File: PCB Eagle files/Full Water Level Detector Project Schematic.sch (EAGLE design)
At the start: 25 parts, among them IC1 74AHCT125, J1 Sensor 1, J2 Sensor 2, J3 Servo

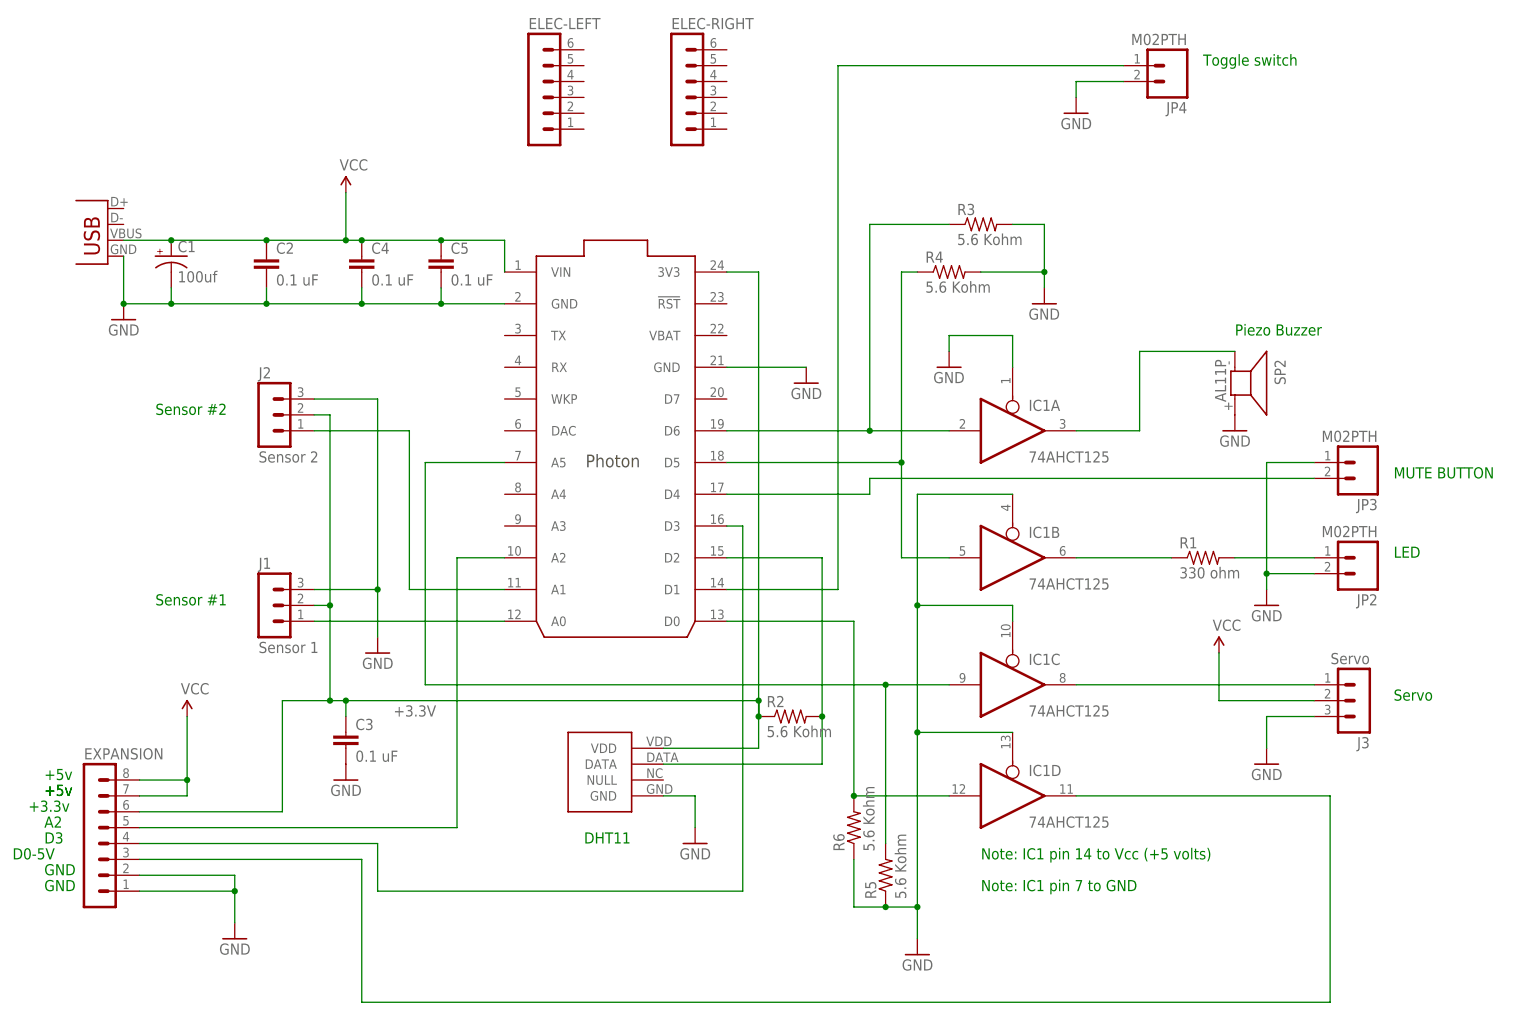
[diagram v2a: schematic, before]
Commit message: Optimized and routed PCB
Still must perform the ground pour and create silk screen.
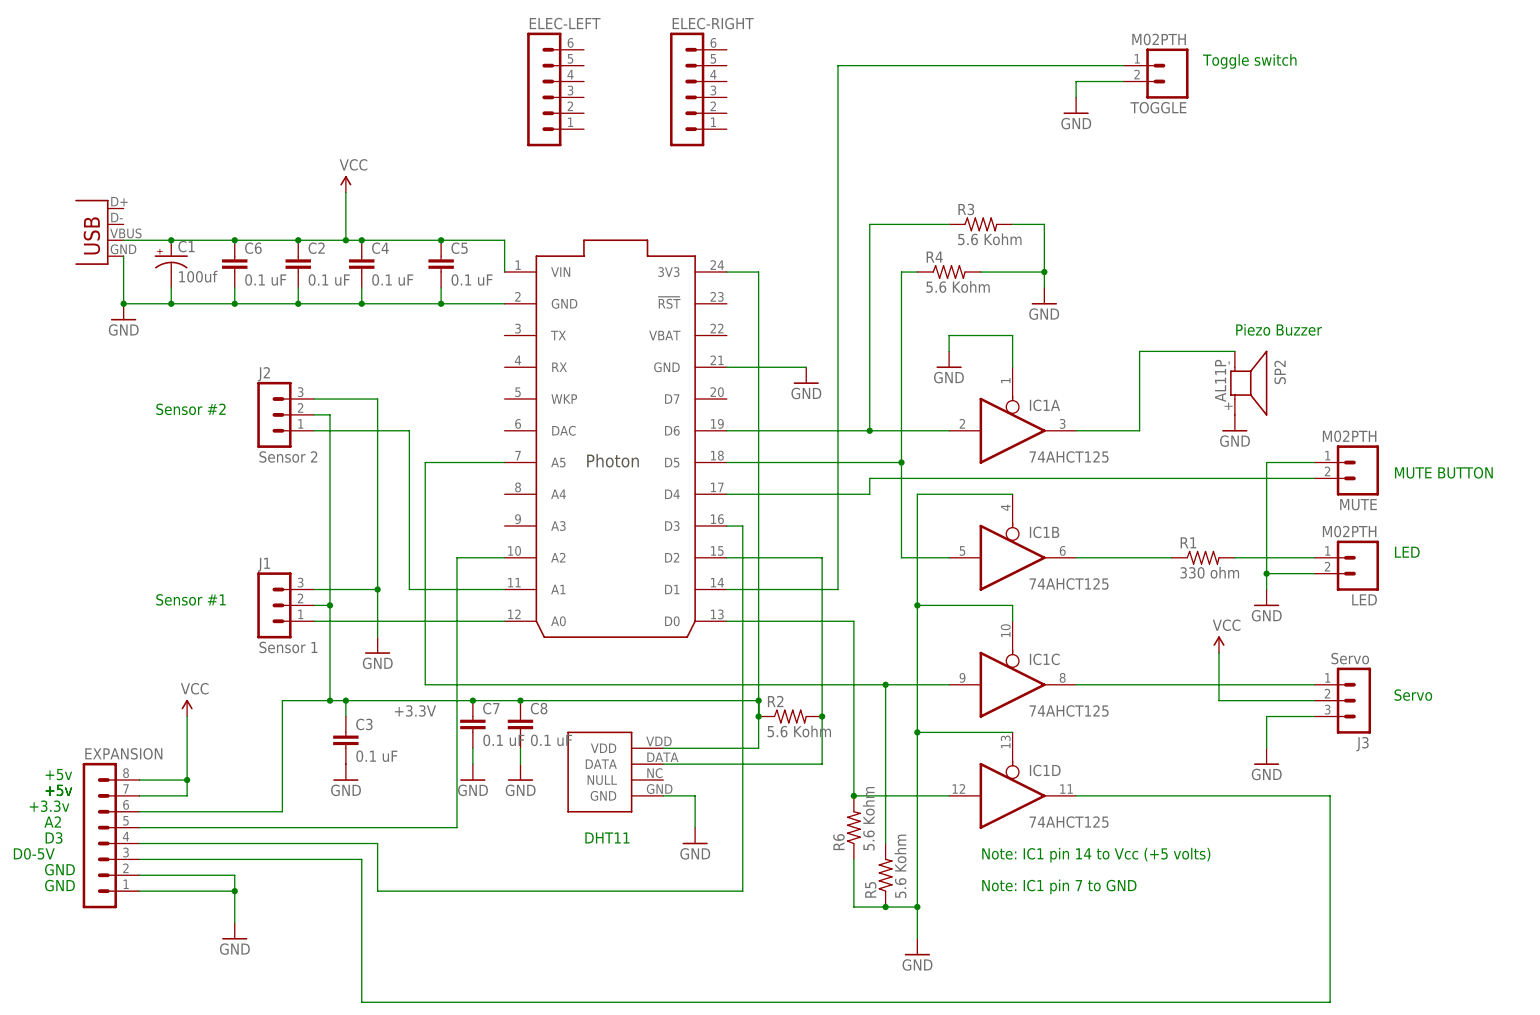
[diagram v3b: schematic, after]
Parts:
- added C6, C7, C8: 0.1 uF, SparkFun-Passives:CAPPTH
- renumbered JP2 to LED, JP3 to MUTE, JP4 to TOGGLE
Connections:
- net +3.3V: now also C7.1, C8.1
- net GND: now also C6.2, C7.2, C8.2
- net VCC: now also C6.1
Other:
- moved on the sheet: C2
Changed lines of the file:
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@@
 <part name="ELEC-LEFT" library="con-lstb" deviceset="MA06-1" device=""/>
 <part name="ELEC-RIGHT" library="con-lstb" deviceset="MA06-1" device=""/>
-<part name="JP3" library="SparkFun-Connectors" deviceset="M02" device="PTH"/>
-<part name="JP2" library="SparkFun-Connectors" deviceset="M02" device="PTH"/>
-<part name="JP4" library="SparkFun-Connectors" deviceset="M02" device="PTH"/>
+<part name="MUTE" library="SparkFun-Connectors" deviceset="M02" device="PTH"/>
+<part name="LED" library="SparkFun-Connectors" deviceset="M02" device="PTH"/>
+<part name="TOGGLE" library="SparkFun-Connectors" deviceset="M02" device="PTH"/>
+<part name="C6" library="SparkFun-Passives" deviceset="CAP" device="PTH" value="0.1 uF"/>
+<part name="C7" library="SparkFun-Passives" deviceset="CAP" device="PTH" value="0.1 uF"/>
+<part name="C8" library="SparkFun-Passives" deviceset="CAP" device="PTH" value="0.1 uF"/>
+<part name="GND14" library="SparkFun-Aesthetics" deviceset="GND" device=""/>
+<part name="GND15" library="SparkFun-Aesthetics" deviceset="GND" device=""/>
 </parts>
 <sheets>
@@
 <instance part="JP1" gate="G$1" x="-88.9" y="96.52" rot="MR0"/>
 <instance part="GND2" gate="1" x="-86.36" y="86.36" rot="MR0"/>
-<instance part="C2" gate="G$1" x="-63.5" y="93.98"/>
+<instance part="C2" gate="G$1" x="-58.42" y="93.98"/>
 <instance part="C3" gate="G$1" x="-50.8" y="17.78"/>
 <instance part="GND3" gate="1" x="-50.8" y="12.7" rot="MR0"/>
@@
 <instance part="ELEC-LEFT" gate="1" x="-20.32" y="124.46"/>
 <instance part="ELEC-RIGHT" gate="1" x="2.54" y="124.46"/>
-<instance part="JP3" gate="G$1" x="111.76" y="63.5" rot="R180"/>
-<instance part="JP2" gate="G$1" x="111.76" y="48.26" rot="R180"/>
-<instance part="JP4" gate="G$1" x="81.28" y="127" rot="R180"/>
+<instance part="MUTE" gate="G$1" x="111.76" y="63.5" rot="R180"/>
+<instance part="LED" gate="G$1" x="111.76" y="48.26" rot="R180"/>
+<instance part="TOGGLE" gate="G$1" x="81.28" y="127" rot="R180"/>
+<instance part="C6" gate="G$1" x="-68.58" y="93.98"/>
+<instance part="C7" gate="G$1" x="-30.48" y="20.32"/>
+<instance part="C8" gate="G$1" x="-22.86" y="20.32"/>
+<instance part="GND14" gate="1" x="-30.48" y="12.7" rot="MR0"/>
+<instance part="GND15" gate="1" x="-22.86" y="12.7" rot="MR0"/>
 </instances>
 <busses>
@@
 <pinref part="JP1" gate="G$1" pin="GND"/>
 <wire x1="-25.4" y1="88.9" x2="-35.56" y2="88.9" width="0.1524" layer="91"/>
-<wire x1="-48.26" y1="88.9" x2="-63.5" y2="88.9" width="0.1524" layer="91"/>
-<wire x1="-63.5" y1="88.9" x2="-78.74" y2="88.9" width="0.1524" layer="91"/>
+<wire x1="-48.26" y1="88.9" x2="-58.42" y2="88.9" width="0.1524" layer="91"/>
+<wire x1="-58.42" y1="88.9" x2="-68.58" y2="88.9" width="0.1524" layer="91"/>
+<wire x1="-68.58" y1="88.9" x2="-78.74" y2="88.9" width="0.1524" layer="91"/>
 <wire x1="-78.74" y1="88.9" x2="-86.36" y2="88.9" width="0.1524" layer="91"/>
 <wire x1="-86.36" y1="88.9" x2="-86.36" y2="96.52" width="0.1524" layer="91"/>
@@
 <junction x="-86.36" y="88.9"/>
 <pinref part="C2" gate="G$1" pin="2"/>
-<wire x1="-63.5" y1="91.44" x2="-63.5" y2="88.9" width="0.1524" layer="91"/>
-<junction x="-63.5" y="88.9"/>
+<wire x1="-58.42" y1="91.44" x2="-58.42" y2="88.9" width="0.1524" layer="91"/>
+<junction x="-58.42" y="88.9"/>
 <pinref part="C4" gate="G$1" pin="2"/>
 <wire x1="-48.26" y1="91.44" x2="-48.26" y2="88.9" width="0.1524" layer="91"/>
@@
 <wire x1="-78.74" y1="91.44" x2="-78.74" y2="88.9" width="0.1524" layer="91"/>
 <junction x="-78.74" y="88.9"/>
+<pinref part="C6" gate="G$1" pin="2"/>
+<wire x1="-68.58" y1="91.44" x2="-68.58" y2="88.9" width="0.1524" layer="91"/>
+<junction x="-68.58" y="88.9"/>
 </segment>
 <segment>
@@
 <wire x1="104.14" y1="45.72" x2="96.52" y2="45.72" width="0.1524" layer="91"/>
 <junction x="96.52" y="45.72"/>
-<pinref part="JP3" gate="G$1" pin="1"/>
-<pinref part="JP2" gate="G$1" pin="2"/>
+<pinref part="MUTE" gate="G$1" pin="1"/>
+<pinref part="LED" gate="G$1" pin="2"/>
 </segment>
 <segment>
@@
 <wire x1="66.04" y1="121.92" x2="66.04" y2="124.46" width="0.1524" layer="91"/>
 <wire x1="66.04" y1="124.46" x2="73.66" y2="124.46" width="0.1524" layer="91"/>
-<pinref part="JP4" gate="G$1" pin="2"/>
+<pinref part="TOGGLE" gate="G$1" pin="2"/>
 </segment>
 <segment>
@@
 <junction x="60.96" y="93.98"/>
 <pinref part="GND10" gate="1" pin="GND"/>
+</segment>
+<segment>
+<pinref part="C7" gate="G$1" pin="2"/>
+<pinref part="GND14" gate="1" pin="GND"/>
+<wire x1="-30.48" y1="17.78" x2="-30.48" y2="15.24" width="0.1524" layer="91"/>
+</segment>
+<segment>
+<pinref part="C8" gate="G$1" pin="2"/>
+<pinref part="GND15" gate="1" pin="GND"/>
+<wire x1="-22.86" y1="17.78" x2="-22.86" y2="15.24" width="0.1524" layer="91"/>
 </segment>
 </net>
@@
 <wire x1="15.24" y1="25.4" x2="15.24" y2="17.78" width="0.1524" layer="91"/>
 <wire x1="15.24" y1="17.78" x2="0" y2="17.78" width="0.1524" layer="91"/>
-<wire x1="15.24" y1="25.4" x2="-50.8" y2="25.4" width="0.1524" layer="91"/>
+<wire x1="15.24" y1="25.4" x2="-22.86" y2="25.4" width="0.1524" layer="91"/>
 <junction x="15.24" y="25.4"/>
 <pinref part="R2" gate="G$1" pin="1"/>
@@
 <label x="-43.18" y="22.86" size="1.778" layer="95"/>
 <pinref part="C3" gate="G$1" pin="1"/>
+<wire x1="-22.86" y1="25.4" x2="-30.48" y2="25.4" width="0.1524" layer="91"/>
+<wire x1="-30.48" y1="25.4" x2="-50.8" y2="25.4" width="0.1524" layer="91"/>
 <wire x1="-50.8" y1="25.4" x2="-50.8" y2="22.86" width="0.1524" layer="91"/>
 <junction x="-50.8" y="25.4"/>
@@
 <pinref part="EXPANSION" gate="1" pin="6"/>
 <wire x1="-83.82" y1="7.62" x2="-60.96" y2="7.62" width="0.1524" layer="91"/>
+<pinref part="C7" gate="G$1" pin="1"/>
+<junction x="-30.48" y="25.4"/>
+<pinref part="C8" gate="G$1" pin="1"/>
+<junction x="-22.86" y="25.4"/>
 </segment>
 </net>
@@
 <pinref part="U$1" gate="G$1" pin="VIN"/>
 <wire x1="-86.36" y1="99.06" x2="-78.74" y2="99.06" width="0.1524" layer="91"/>
-<wire x1="-78.74" y1="99.06" x2="-63.5" y2="99.06" width="0.1524" layer="91"/>
-<wire x1="-63.5" y1="99.06" x2="-50.8" y2="99.06" width="0.1524" layer="91"/>
+<wire x1="-78.74" y1="99.06" x2="-68.58" y2="99.06" width="0.1524" layer="91"/>
+<wire x1="-68.58" y1="99.06" x2="-58.42" y2="99.06" width="0.1524" layer="91"/>
+<wire x1="-58.42" y1="99.06" x2="-50.8" y2="99.06" width="0.1524" layer="91"/>
 <wire x1="-50.8" y1="99.06" x2="-48.26" y2="99.06" width="0.1524" layer="91"/>
 <wire x1="-48.26" y1="99.06" x2="-35.56" y2="99.06" width="0.1524" layer="91"/>
@@
 <wire x1="-25.4" y1="99.06" x2="-25.4" y2="93.98" width="0.1524" layer="91"/>
 <pinref part="C2" gate="G$1" pin="1"/>
-<junction x="-63.5" y="99.06"/>
+<junction x="-58.42" y="99.06"/>
 <pinref part="SUPPLY1" gate="1" pin="VCC"/>
 <wire x1="-50.8" y1="106.68" x2="-50.8" y2="99.06" width="0.1524" layer="91"/>
@@
 <pinref part="C1" gate="G$1" pin="+"/>
 <junction x="-78.74" y="99.06"/>
+<pinref part="C6" gate="G$1" pin="1"/>
+<junction x="-68.58" y="99.06"/>
 </segment>
 <segment>
@@
 <pinref part="U$1" gate="G$1" pin="D4"/>
 <wire x1="10.16" y1="58.42" x2="33.02" y2="58.42" width="0.1524" layer="91"/>
-<pinref part="JP3" gate="G$1" pin="2"/>
+<pinref part="MUTE" gate="G$1" pin="2"/>
 </segment>
 </net>
@@
 <wire x1="10.16" y1="43.18" x2="27.94" y2="43.18" width="0.1524" layer="91"/>
 <wire x1="27.94" y1="127" x2="73.66" y2="127" width="0.1524" layer="91"/>
-<pinref part="JP4" gate="G$1" pin="1"/>
+<pinref part="TOGGLE" gate="G$1" pin="1"/>
 </segment>
 </net>
@@
 <pinref part="R1" gate="G$1" pin="2"/>
 <wire x1="104.14" y1="48.26" x2="91.44" y2="48.26" width="0.1524" layer="91"/>
-<pinref part="JP2" gate="G$1" pin="1"/>
-</segment>
-</net>
+<pinref part="LED" gate="G$1" pin="1"/>
+</segment>
+</net>
